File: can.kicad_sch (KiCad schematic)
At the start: 20 parts, among them U7 TJA1051T-3, U8 MCP2510-x/SO, Y2 16MHz

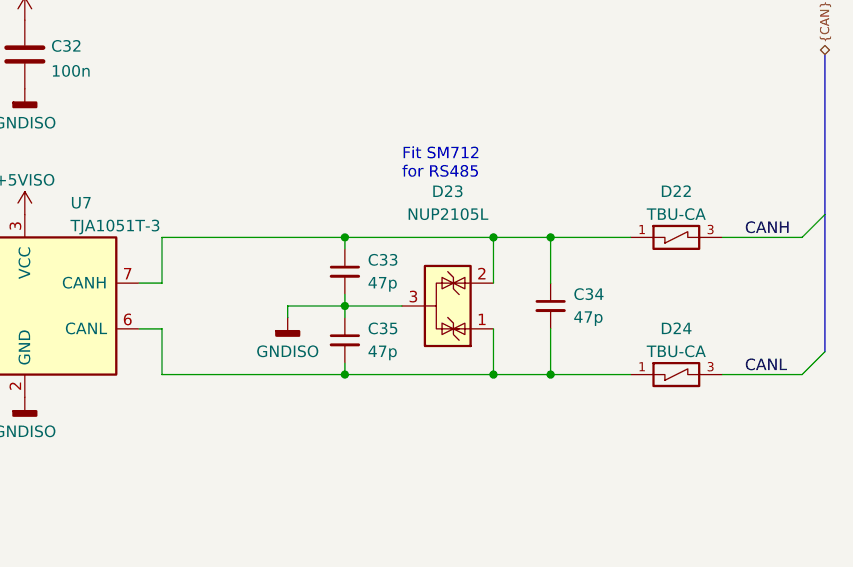
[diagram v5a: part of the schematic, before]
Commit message: Minimal design for testing
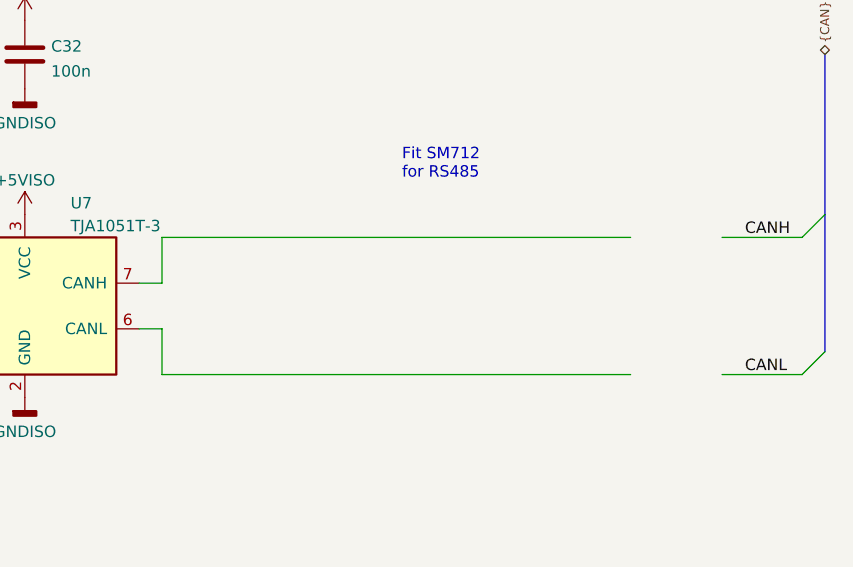
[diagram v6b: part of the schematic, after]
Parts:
- removed C33, C34, C35: 47p, Capacitor_SMD:C_0603_1608Metric, symbol Device:C_Small
- removed D22, D24: TBU-CA, TBU-CA:DIOC650X400X100N, symbol TBU-CA065-200-WH:TBU-CA065-200-WH
- removed D23: NUP2105L, Package_TO_SOT_SMD:SOT-23, symbol Power_Protection:NUP2105L
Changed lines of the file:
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@@
   (junction (at 38.1 106.68) (diameter 0) (color 0 0 0 0)
   )
-  (junction (at 248.92 99.06) (diameter 0) (color 0 0 0 0)
-  )
-  (junction (at 226.06 91.44) (diameter 0) (color 0 0 0 0)
-  )
   (junction (at 68.58 104.14) (diameter 0) (color 0 0 0 0)
   )
   (junction (at 57.15 111.76) (diameter 0) (color 0 0 0 0)
   )
-  (junction (at 242.57 83.82) (diameter 0) (color 0 0 0 0)
-  )
-  (junction (at 242.57 99.06) (diameter 0) (color 0 0 0 0)
-  )
-  (junction (at 226.06 99.06) (diameter 0) (color 0 0 0 0)
-  )
   (junction (at 38.1 111.76) (diameter 0) (color 0 0 0 0)
-  )
-  (junction (at 248.92 83.82) (diameter 0) (color 0 0 0 0)
-  )
-  (junction (at 226.06 83.82) (diameter 0) (color 0 0 0 0)
   )
   (junction (at 179.07 118.11) (diameter 0) (color 0 0 0 0)
@@
     (stroke (width 0) (type default) (color 0 0 0 0))
   )
-  (wire (pts (xy 242.57 93.98) (xy 242.57 99.06))
-    (stroke (width 0) (type default) (color 0 0 0 0))
-  )
   (bus (pts (xy 279.4 81.28) (xy 279.4 63.5))
     (stroke (width 0) (type default) (color 0 0 0 0))
   )
-  (wire (pts (xy 219.71 91.44) (xy 226.06 91.44))
-    (stroke (width 0) (type default) (color 0 0 0 0))
-  )
   (wire (pts (xy 177.8 88.9) (xy 158.75 88.9))
     (stroke (width 0) (type default) (color 0 0 0 0))
@@
     (stroke (width 0) (type default) (color 0 0 0 0))
   )
-  (wire (pts (xy 226.06 83.82) (xy 242.57 83.82))
-    (stroke (width 0) (type default) (color 0 0 0 0))
-  )
   (wire (pts (xy 60.96 86.36) (xy 86.36 86.36))
     (stroke (width 0) (type default) (color 0 0 0 0))
@@
     (stroke (width 0) (type default) (color 0 0 0 0))
   )
-  (wire (pts (xy 248.92 83.82) (xy 257.81 83.82))
-    (stroke (width 0) (type default) (color 0 0 0 0))
-  )
   (wire (pts (xy 116.84 101.6) (xy 127 101.6))
     (stroke (width 0) (type default) (color 0 0 0 0))
   )
-  (wire (pts (xy 226.06 91.44) (xy 226.06 92.71))
-    (stroke (width 0) (type default) (color 0 0 0 0))
-  )
   (bus (pts (xy 279.4 81.28) (xy 279.4 96.52))
     (stroke (width 0) (type default) (color 0 0 0 0))
@@
     (stroke (width 0) (type default) (color 0 0 0 0))
   )
-  (wire (pts (xy 242.57 99.06) (xy 248.92 99.06))
-    (stroke (width 0) (type default) (color 0 0 0 0))
-  )
   (wire (pts (xy 116.84 86.36) (xy 133.35 86.36))
     (stroke (width 0) (type default) (color 0 0 0 0))
@@
     (stroke (width 0) (type default) (color 0 0 0 0))
   )
-  (wire (pts (xy 205.74 99.06) (xy 226.06 99.06))
+  (wire (pts (xy 205.74 99.06) (xy 257.81 99.06))
     (stroke (width 0) (type default) (color 0 0 0 0))
   )
@@
     (stroke (width 0) (type default) (color 0 0 0 0))
   )
-  (wire (pts (xy 248.92 83.82) (xy 248.92 88.9))
-    (stroke (width 0) (type default) (color 0 0 0 0))
-  )
   (wire (pts (xy 68.58 111.76) (xy 68.58 109.22))
     (stroke (width 0) (type default) (color 0 0 0 0))
@@
     (stroke (width 0) (type default) (color 0 0 0 0))
   )
-  (wire (pts (xy 226.06 99.06) (xy 242.57 99.06))
-    (stroke (width 0) (type default) (color 0 0 0 0))
-  )
   (wire (pts (xy 57.15 111.76) (xy 68.58 111.76))
     (stroke (width 0) (type default) (color 0 0 0 0))
@@
     (stroke (width 0) (type default) (color 0 0 0 0))
   )
-  (wire (pts (xy 248.92 99.06) (xy 257.81 99.06))
-    (stroke (width 0) (type default) (color 0 0 0 0))
-  )
-  (wire (pts (xy 219.71 92.71) (xy 219.71 91.44))
-    (stroke (width 0) (type default) (color 0 0 0 0))
-  )
-  (wire (pts (xy 248.92 93.98) (xy 248.92 99.06))
-    (stroke (width 0) (type default) (color 0 0 0 0))
-  )
   (wire (pts (xy 203.2 88.9) (xy 205.74 88.9))
     (stroke (width 0) (type default) (color 0 0 0 0))
   )
-  (wire (pts (xy 226.06 91.44) (xy 232.41 91.44))
-    (stroke (width 0) (type default) (color 0 0 0 0))
-  )
-  (wire (pts (xy 242.57 83.82) (xy 248.92 83.82))
-    (stroke (width 0) (type default) (color 0 0 0 0))
-  )
   (wire (pts (xy 177.8 93.98) (xy 170.18 93.98))
     (stroke (width 0) (type default) (color 0 0 0 0))
@@
     (stroke (width 0) (type default) (color 0 0 0 0))
   )
-  (wire (pts (xy 226.06 83.82) (xy 226.06 85.09))
-    (stroke (width 0) (type default) (color 0 0 0 0))
-  )
   (wire (pts (xy 205.74 93.98) (xy 205.74 99.06))
     (stroke (width 0) (type default) (color 0 0 0 0))
@@
     (stroke (width 0) (type default) (color 0 0 0 0))
   )
-  (wire (pts (xy 226.06 97.79) (xy 226.06 99.06))
-    (stroke (width 0) (type default) (color 0 0 0 0))
-  )
-  (wire (pts (xy 242.57 83.82) (xy 242.57 88.9))
-    (stroke (width 0) (type default) (color 0 0 0 0))
-  )
-  (wire (pts (xy 205.74 83.82) (xy 226.06 83.82))
+  (wire (pts (xy 205.74 83.82) (xy 257.81 83.82))
     (stroke (width 0) (type default) (color 0 0 0 0))
   )
   (wire (pts (xy 60.96 91.44) (xy 86.36 91.44))
-    (stroke (width 0) (type default) (color 0 0 0 0))
-  )
-  (wire (pts (xy 226.06 90.17) (xy 226.06 91.44))
     (stroke (width 0) (type default) (color 0 0 0 0))
   )
@@
     (pin "1")
   )
-  (symbol (lib_id "Device:C_Small") (at 226.06 87.63 0) (unit 1)
-    (in_bom yes) (on_board yes)
-    (property "Reference" "C33" (id 0) (at 228.6 86.36 0)
-      (effects (font (size 1.27 1.27)) (justify left))
-    )
-    (property "Value" "47p" (id 1) (at 228.6 88.9 0)
-      (effects (font (size 1.27 1.27)) (justify left))
-    )
-    (property "Footprint" "Capacitor_SMD:C_0603_1608Metric" (id 2) (at 226.06 87.63 0)
-      (effects (font (size 1.27 1.27)) hide)
-    )
-    (property "Datasheet" "~" (id 3) (at 226.06 87.63 0)
-      (effects (font (size 1.27 1.27)) hide)
-    )
-    (pin "1")
-    (pin "2")
-  )
   (symbol (lib_id "power_symbols:GNDISO") (at 163.83 93.98 0) (unit 1)
     (in_bom yes) (on_board yes)
@@
     )
     (pin "1")
-  )
-  (symbol (lib_id "TBU-CA065-200-WH:TBU-CA065-200-WH") (at 262.89 99.06 0) (unit 1)
-    (in_bom yes) (on_board yes)
-    (property "Reference" "D24" (id 0) (at 262.89 93.98 0))
-    (property "Value" "TBU-CA" (id 1) (at 262.89 96.52 0))
-    (property "Footprint" "TBU-CA:DIOC650X400X100N" (id 2) (at 262.89 99.06 0)
-      (effects (font (size 1.27 1.27)) (justify left bottom) hide)
-    )
-    (property "Datasheet" "" (id 3) (at 262.89 99.06 0)
-      (effects (font (size 1.27 1.27)) (justify left bottom) hide)
-    )
-    (pin "1")
-    (pin "3")
   )
   (symbol (lib_id "Jumper:Jumper_2_Open") (at 179.07 113.03 270) (unit 1)
@@
     (pin "9")
   )
-  (symbol (lib_id "TBU-CA065-200-WH:TBU-CA065-200-WH") (at 262.89 83.82 0) (unit 1)
-    (in_bom yes) (on_board yes)
-    (property "Reference" "D22" (id 0) (at 262.89 78.74 0))
-    (property "Value" "TBU-CA" (id 1) (at 262.89 81.28 0))
-    (property "Footprint" "TBU-CA:DIOC650X400X100N" (id 2) (at 262.89 83.82 0)
-      (effects (font (size 1.27 1.27)) (justify left bottom) hide)
-    )
-    (property "Datasheet" "" (id 3) (at 262.89 83.82 0)
-      (effects (font (size 1.27 1.27)) (justify left bottom) hide)
-    )
-    (pin "1")
-    (pin "3")
-  )
   (symbol (lib_id "power:GND") (at 128.27 93.98 0) (unit 1)
     (in_bom yes) (on_board yes)
@@
     (pin "2")
   )
-  (symbol (lib_id "power_symbols:GNDISO") (at 219.71 92.71 0) (unit 1)
-    (in_bom yes) (on_board yes)
-    (property "Reference" "#PWR0138" (id 0) (at 219.71 99.06 0)
-      (effects (font (size 1.27 1.27)) hide)
-    )
-    (property "Value" "GNDISO" (id 1) (at 219.71 96.52 0))
-    (property "Footprint" "" (id 2) (at 219.71 92.71 0)
-      (effects (font (size 1.27 1.27)) hide)
-    )
-    (property "Datasheet" "" (id 3) (at 219.71 92.71 0)
-      (effects (font (size 1.27 1.27)) hide)
-    )
-    (pin "1")
-  )
   (symbol (lib_id "power:GND") (at 101.6 67.31 0) (unit 1)
     (in_bom yes) (on_board yes)
@@
     (pin "2")
   )
-  (symbol (lib_id "Power_Protection:NUP2105L") (at 237.49 91.44 270) (mirror x) (unit 1)
-    (in_bom yes) (on_board yes)
-    (property "Reference" "D23" (id 0) (at 237.49 78.74 90))
-    (property "Value" "NUP2105L" (id 1) (at 237.49 81.28 90))
-    (property "Footprint" "Package_TO_SOT_SMD:SOT-23" (id 2) (at 236.22 85.725 0)
-      (effects (font (size 1.27 1.27)) (justify left) hide)
-    )
-    (property "Datasheet" "http://www.onsemi.com/pub_link/Collateral/NUP2105L-D.PDF" (id 3) (at 240.665 88.265 0)
-      (effects (font (size 1.27 1.27)) hide)
-    )
-    (pin "3")
-    (pin "1")
-    (pin "2")
-  )
   (symbol (lib_id "power_symbols:GNDISO") (at 190.5 101.6 0) (unit 1)
     (in_bom yes) (on_board yes)
@@
     (pin "1")
   )
-  (symbol (lib_id "Device:C_Small") (at 248.92 91.44 0) (unit 1)
-    (in_bom yes) (on_board yes)
-    (property "Reference" "C34" (id 0) (at 251.46 90.17 0)
-      (effects (font (size 1.27 1.27)) (justify left))
-    )
-    (property "Value" "47p" (id 1) (at 251.46 92.71 0)
-      (effects (font (size 1.27 1.27)) (justify left))
-    )
-    (property "Footprint" "Capacitor_SMD:C_0603_1608Metric" (id 2) (at 248.92 91.44 0)
-      (effects (font (size 1.27 1.27)) hide)
-    )
-    (property "Datasheet" "~" (id 3) (at 248.92 91.44 0)
-      (effects (font (size 1.27 1.27)) hide)
-    )
-    (pin "1")
-    (pin "2")
-  )
   (symbol (lib_id "power_symbols:+5VISO") (at 179.07 107.95 0) (unit 1)
     (in_bom yes) (on_board yes)
@@
     (pin "1")
   )
-  (symbol (lib_id "Device:C_Small") (at 226.06 95.25 0) (unit 1)
-    (in_bom yes) (on_board yes)
-    (property "Reference" "C35" (id 0) (at 228.6 93.98 0)
-      (effects (font (size 1.27 1.27)) (justify left))
-    )
-    (property "Value" "47p" (id 1) (at 228.6 96.52 0)
-      (effects (font (size 1.27 1.27)) (justify left))
-    )
-    (property "Footprint" "Capacitor_SMD:C_0603_1608Metric" (id 2) (at 226.06 95.25 0)
-      (effects (font (size 1.27 1.27)) hide)
-    )
-    (property "Datasheet" "~" (id 3) (at 226.06 95.25 0)
-      (effects (font (size 1.27 1.27)) hide)
-    )
-    (pin "1")
-    (pin "2")
-  )
   (symbol (lib_id "Device:C") (at 44.45 101.6 90) (mirror x) (unit 1)
